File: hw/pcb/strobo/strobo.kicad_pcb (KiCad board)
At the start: 2 copper layers, 91 parts, among them J1 Conn_ARM_JTAG_SWD_10, SW1 SW_SPST, U1 ICM-20602, U2 STM32L051K8Ux, Y1 32kHz

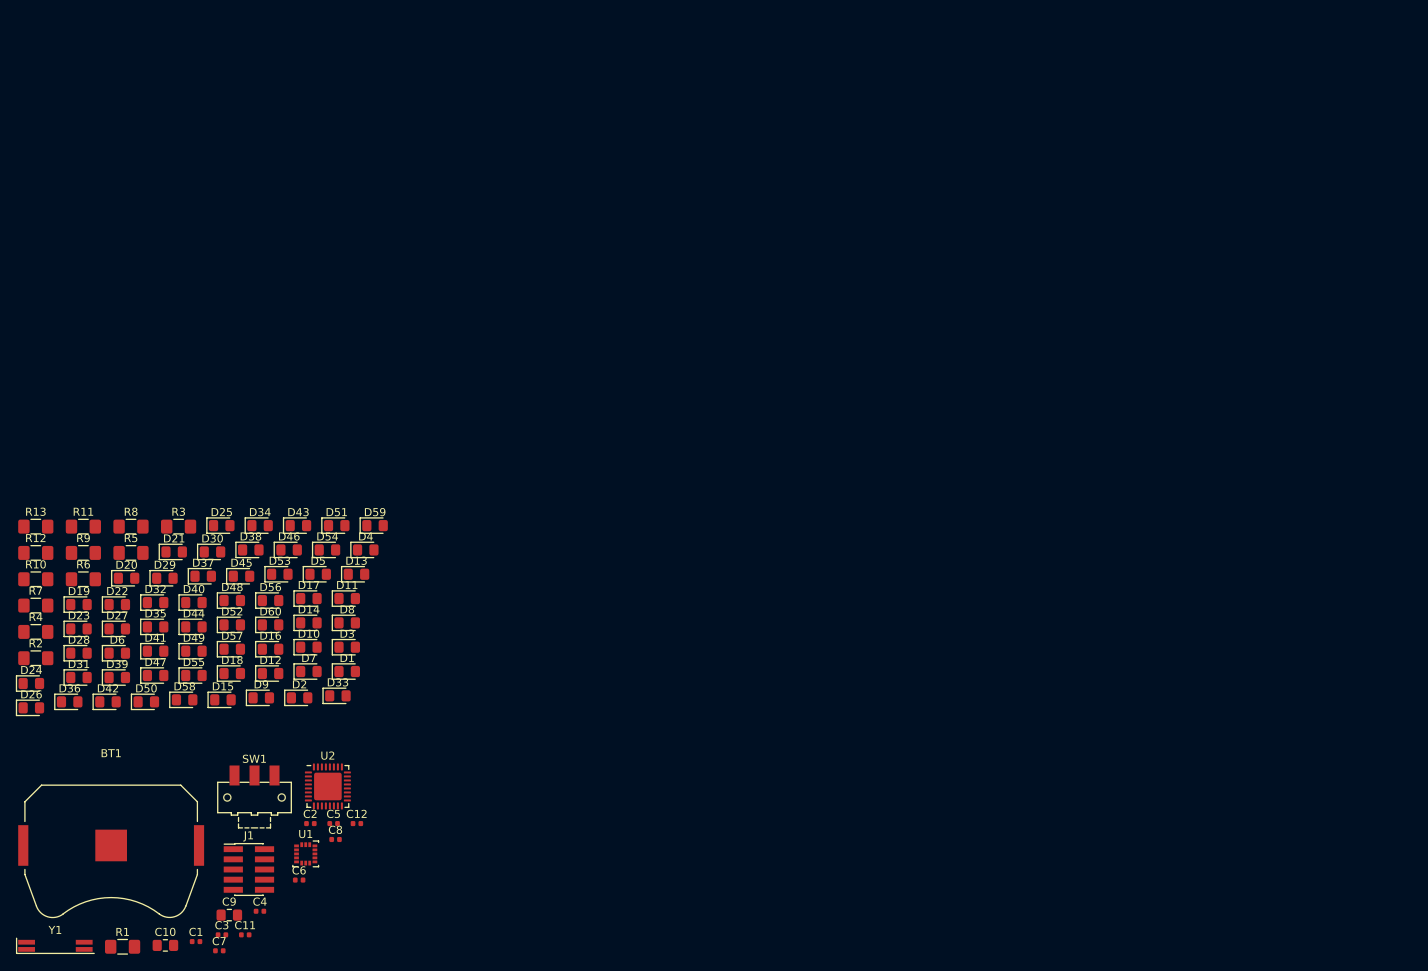
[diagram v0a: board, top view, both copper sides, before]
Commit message: initial led placement
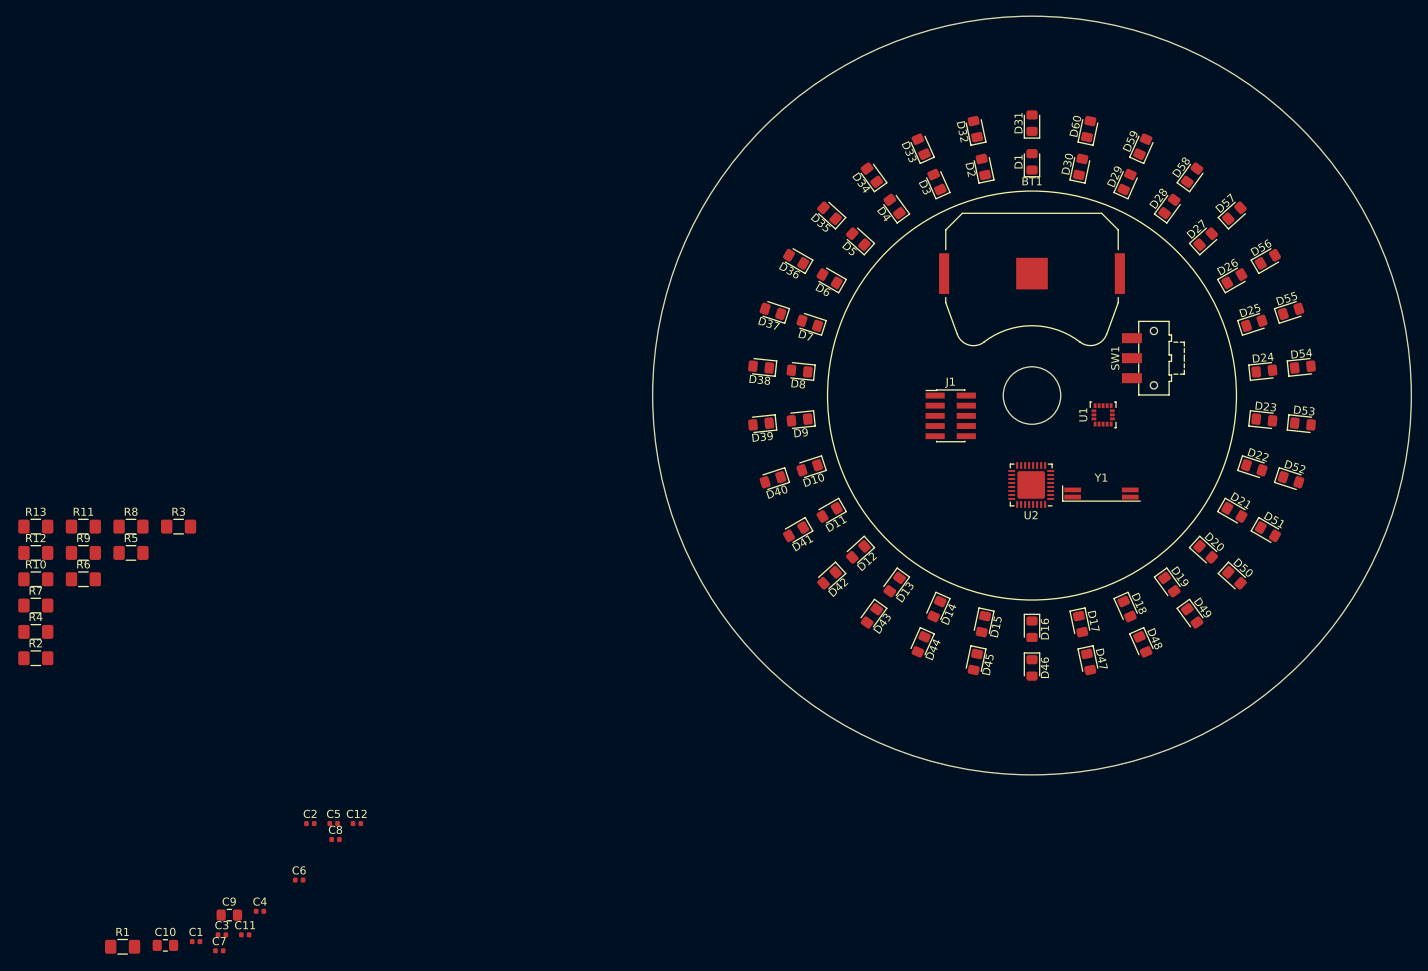
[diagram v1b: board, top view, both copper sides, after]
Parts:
- moved D26 159.7 mm to (226.0, 85.7), turned to 30 degrees
- moved D24 159.0 mm to (229.7, 97.3), turned to 6 degrees
- moved D23 150.5 mm to (229.7, 103.4), turned to 354 degrees
- moved D28 147.3 mm to (217.8, 76.7), turned to 54 degrees
- moved D27 144.5 mm to (222.4, 80.8), turned to 42 degrees
- moved D55 144.5 mm to (233.0, 89.8), turned to 18 degrees
- moved D22 143.1 mm to (228.4, 109.4), turned to 342 degrees
- moved Y1 142.5 mm to (209.3, 112.6)
- moved D58 142.0 mm to (220.7, 72.8), turned to 54 degrees
- moved D31 137.8 mm to (200.7, 66.3), turned to 90 degrees
- moved D50 136.9 mm to (226.0, 123.1), turned to 318 degrees
- moved D57 136.6 mm to (226.0, 77.5), turned to 42 degrees
- moved D19 136.3 mm to (217.8, 124.0), turned to 306 degrees
- moved BT1 135.5 mm to (200.7, 85.1)
- moved D20 134.9 mm to (222.4, 119.9), turned to 318 degrees
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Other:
- board outline added: 94.8 x 94.8 mm

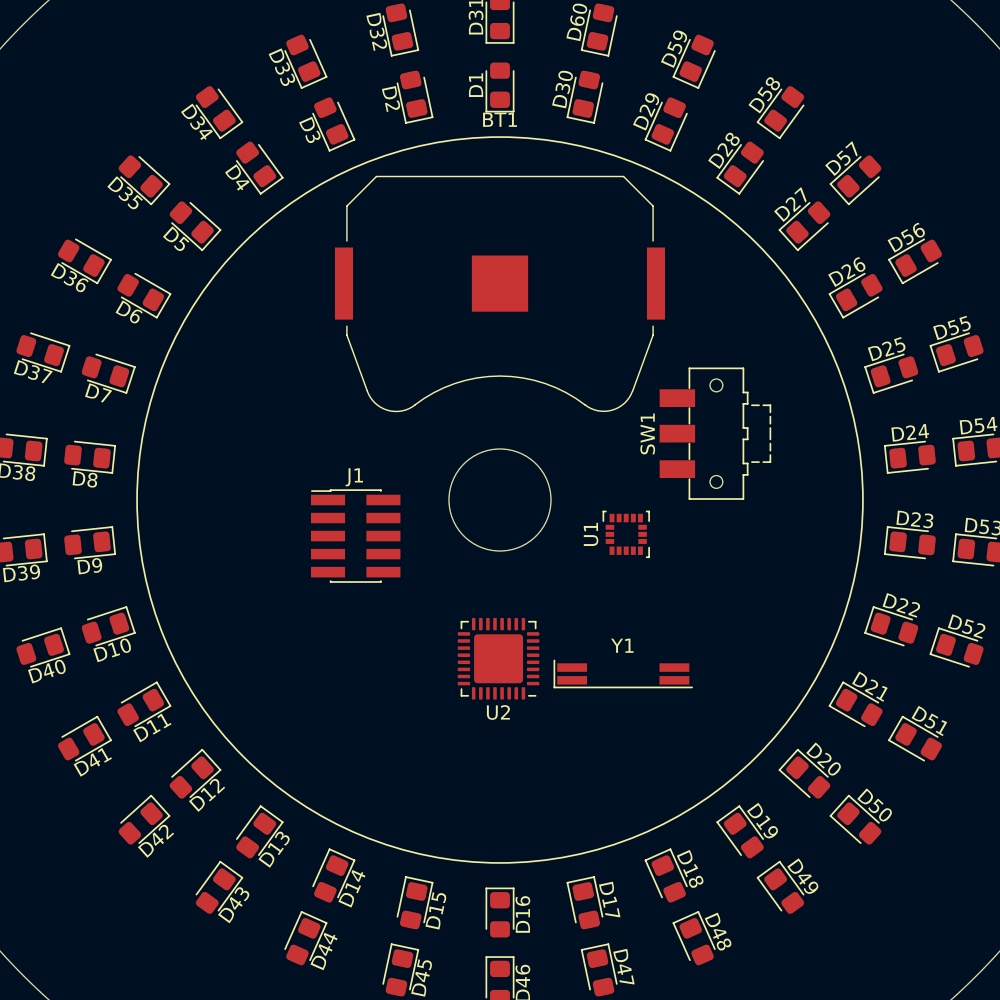
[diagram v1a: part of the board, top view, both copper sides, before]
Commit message: led tracks for inner ring
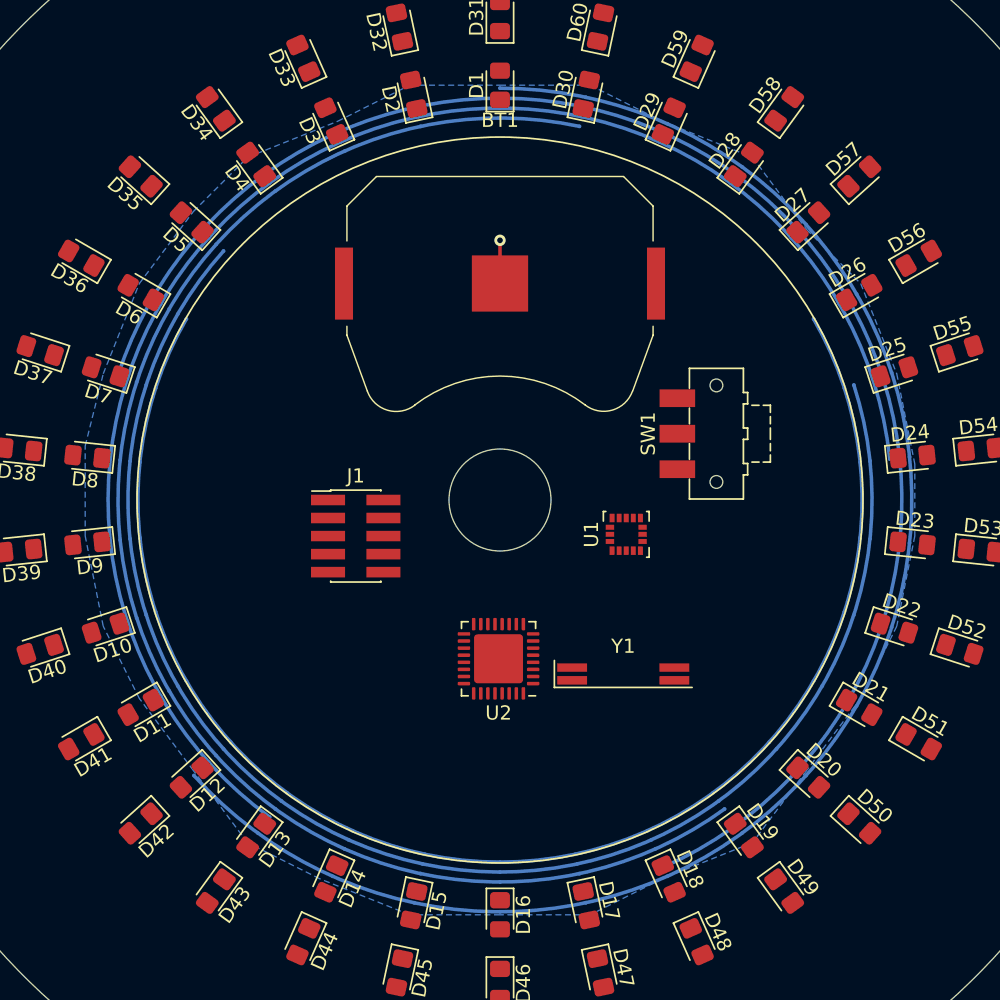
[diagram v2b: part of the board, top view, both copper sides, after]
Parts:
- added LED_Ring_Track: LED_Ring, strobo:LED_Ring, B.Cu at (200.7, 100.3)
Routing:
- net GND: track 0.00 -> 3.05 mm, vias 0 -> 1
- added copper zone on B.Cu, net GND
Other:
- net class Default: clearance 0.2 -> 0.1524
- rule trace_clearance: 0.2 -> 0.1524
- rule trace_min: 0.2 -> 0.1524
- rule via_min_drill: 0.3 -> 0.254
- rule via_min_size: 0.4 -> 0.508

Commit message: outer ring
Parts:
- turned LED_Ring_Track to 93 degrees
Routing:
- removed copper zone on B.Cu, net GND

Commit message: map ring tracks to schematic
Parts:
- removed LED_Ring_Track: LED_Ring, strobo:LED_Ring
- added U3: Ring_Tracks, strobo:LED_Ring, B.Cu at (200.7, 100.3)

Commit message: major routing
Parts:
- moved R13 146.5 mm to (219.7, 87.6), turned to 90 degrees
- moved R7 146.3 mm to (217.2, 87.6), turned to 90 degrees
- moved R12 143.7 mm to (219.7, 113.0), turned to 90 degrees
- moved R1 141.0 mm to (213.4, 106.7), turned to 180 degrees
- moved R6 135.5 mm to (217.2, 113.0), turned to 90 degrees
- moved R4 132.6 mm to (208.3, 119.4), turned to 180 degrees
- moved R10 132.2 mm to (208.3, 121.9), turned to 180 degrees
- moved C7 127.0 mm to (207.8, 104.1)
- moved C1 123.8 mm to (208.5, 116.6)
- moved C11 117.8 mm to (206.2, 112.3), turned to 180 degrees
- moved C10 117.7 mm to (194.1, 109.9)
- moved R2 117.2 mm to (184.2, 87.6), turned to 90 degrees
- moved C3 114.4 mm to (196.1, 106.7), turned to 180 degrees
- moved C6 113.2 mm to (207.8, 105.4), turned to 180 degrees
- moved C9 112.6 mm to (202.8, 118.6), turned to 90 degrees
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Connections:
- net /LED Matrix/LM_R_A renamed RA
- C6 pad 1: VDD -> Net-(C10-Pad2)
- C7 pad 2: VDD -> Net-(C10-Pad2)
- C8 pad 1: VDD -> Net-(C10-Pad2)
- D1 pad 1: /LED Matrix/LM_R_B -> RB
- D10 pad 1: /LED Matrix/LM_R_F -> RF
- D12 pad 1: /LED Matrix/LM_R_B -> RB
- D13 pad 1: /LED Matrix/LM_R_D -> RD
- D14 pad 1: /LED Matrix/LM_R_E -> RE
- D15 pad 1: /LED Matrix/LM_R_F -> RF
- D17 pad 1: /LED Matrix/LM_R_B -> RB
- D18 pad 1: /LED Matrix/LM_R_C -> RC
- D19 pad 1: /LED Matrix/LM_R_E -> RE
- D2 pad 1: /LED Matrix/LM_R_C -> RC
- D20 pad 1: /LED Matrix/LM_R_F -> RF
- D22 pad 1: /LED Matrix/LM_R_B -> RB
- D23 pad 1: /LED Matrix/LM_R_C -> RC
- D24 pad 1: /LED Matrix/LM_R_D -> RD
- D25 pad 1: /LED Matrix/LM_R_F -> RF
- D27 pad 1: /LED Matrix/LM_R_B -> RB
- D28 pad 1: /LED Matrix/LM_R_C -> RC
- D29 pad 1: /LED Matrix/LM_R_D -> RD
- D3 pad 1: /LED Matrix/LM_R_D -> RD
- D30 pad 1: /LED Matrix/LM_R_E -> RE
- D31 pad 1: /LED Matrix/LM_S_B -> SB
- D32 pad 1: /LED Matrix/LM_S_C -> SC
- D33 pad 1: /LED Matrix/LM_S_D -> SD
- D34 pad 1: /LED Matrix/LM_S_E -> SE
- D35 pad 1: /LED Matrix/LM_S_F -> SF
- D36 pad 1: /LED Matrix/LM_S_A -> SA
- D37 pad 1: /LED Matrix/LM_S_C -> SC
- D38 pad 1: /LED Matrix/LM_S_D -> SD
- D39 pad 1: /LED Matrix/LM_S_E -> SE
- D4 pad 1: /LED Matrix/LM_R_E -> RE
- D40 pad 1: /LED Matrix/LM_S_F -> SF
- D41 pad 1: /LED Matrix/LM_S_A -> SA
- D42 pad 1: /LED Matrix/LM_S_B -> SB
- D43 pad 1: /LED Matrix/LM_S_D -> SD
- D44 pad 1: /LED Matrix/LM_S_E -> SE
- D45 pad 1: /LED Matrix/LM_S_F -> SF
- D46 pad 1: /LED Matrix/LM_S_A -> SA
- D47 pad 1: /LED Matrix/LM_S_B -> SB
- D48 pad 1: /LED Matrix/LM_S_C -> SC
- D49 pad 1: /LED Matrix/LM_S_E -> SE
- D5 pad 1: /LED Matrix/LM_R_F -> RF
- D50 pad 1: /LED Matrix/LM_S_F -> SF
- D51 pad 1: /LED Matrix/LM_S_A -> SA
- D52 pad 1: /LED Matrix/LM_S_B -> SB
- D53 pad 1: /LED Matrix/LM_S_C -> SC
- D54 pad 1: /LED Matrix/LM_S_D -> SD
- D55 pad 1: /LED Matrix/LM_S_F -> SF
- D56 pad 1: /LED Matrix/LM_S_A -> SA
- D57 pad 1: /LED Matrix/LM_S_B -> SB
- D58 pad 1: /LED Matrix/LM_S_C -> SC
- D59 pad 1: /LED Matrix/LM_S_D -> SD
- D60 pad 1: /LED Matrix/LM_S_E -> SE
- D7 pad 1: /LED Matrix/LM_R_C -> RC
- D8 pad 1: /LED Matrix/LM_R_D -> RD
- D9 pad 1: /LED Matrix/LM_R_E -> RE
- R10 pad 1: /LED Matrix/LM_S_C -> SC
- R11 pad 1: /LED Matrix/LM_S_D -> SD
- R12 pad 1: /LED Matrix/LM_S_E -> SE
- R13 pad 1: /LED Matrix/LM_S_F -> SF
- R3 pad 1: /LED Matrix/LM_R_B -> RB
- R4 pad 1: /LED Matrix/LM_R_C -> RC
- R5 pad 1: /LED Matrix/LM_R_D -> RD
- R6 pad 1: /LED Matrix/LM_R_E -> RE
- R7 pad 1: /LED Matrix/LM_R_F -> RF
- R8 pad 1: /LED Matrix/LM_S_A -> SA
- R9 pad 1: /LED Matrix/LM_S_B -> SB
- U1 pad 1: VDD -> Net-(C10-Pad2)
- U1 pad 16: VDD -> Net-(C10-Pad2)
- U2 pad 19: /LED Matrix/LM_R_B -> SA
- U2 pad 20: /LED Matrix/LM_R_C -> RB
- U2 pad 21: /LED Matrix/LM_R_D -> SB
- U2 pad 22: /LED Matrix/LM_R_E -> RD
- U2 pad 25: /LED Matrix/LM_R_F -> SD
- U2 pad 26: /LED Matrix/LM_S_F -> RC
- U2 pad 27: /LED Matrix/LM_S_E -> SC
- U2 pad 28: /LED Matrix/LM_S_D -> RE
- U2 pad 29: /LED Matrix/LM_S_C -> Net-(U2-Pad29)
- U2 pad 30: /LED Matrix/LM_S_B -> Net-(U2-Pad30)
- U2 pad 32: /LED Matrix/LM_S_A -> Net-(U2-Pad32)
- U2 pad 6: Net-(U2-Pad6) -> SE
- U2 pad 7: Net-(U2-Pad7) -> RF
- U2 pad 8: Net-(U2-Pad8) -> SF
- U3 pad 10: /LED Matrix/LM_S_D -> SD
- U3 pad 11: /LED Matrix/LM_S_E -> SE
- U3 pad 12: /LED Matrix/LM_S_F -> SF
- U3 pad 13: /LED Matrix/LM_S_A -> SA
- U3 pad 2: /LED Matrix/LM_R_F -> RF
- U3 pad 3: /LED Matrix/LM_R_E -> RE
- U3 pad 4: /LED Matrix/LM_R_D -> RD
- U3 pad 5: /LED Matrix/LM_R_C -> RC
- U3 pad 6: /LED Matrix/LM_R_B -> RB
- U3 pad 8: /LED Matrix/LM_S_B -> SB
- U3 pad 9: /LED Matrix/LM_S_C -> SC
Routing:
- net SA: track 0.00 -> 64.9 mm, vias 0 -> 5
- net SF: track 0.00 -> 59.3 mm, vias 0 -> 6
- net Net-(C10-Pad2): track 0.00 -> 57.3 mm, vias 0 -> 8
- net SB: track 0.00 -> 56.4 mm, vias 0 -> 5
- net RA: track 0.00 -> 55.9 mm, vias 0 -> 5
- net RF: track 0.00 -> 48.1 mm, vias 0 -> 6
- net SC: track 0.00 -> 42.9 mm, vias 0 -> 7
- net VDD: track 0.00 -> 42.0 mm
- net SE: track 0.00 -> 39.9 mm, vias 0 -> 5
- net RB: track 0.00 -> 36.5 mm, vias 0 -> 5
- net RE: track 0.00 -> 34.8 mm, vias 0 -> 7
- net RC: track 0.00 -> 34.6 mm, vias 0 -> 7
- net SD: track 0.00 -> 33.4 mm, vias 0 -> 5
- net Net-(D41-Pad2): track 0.00 -> 32.4 mm, vias 0 -> 7
- net Net-(D46-Pad2): track 0.00 -> 27.4 mm, vias 0 -> 5
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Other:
- board size 94.8 x 94.8 mm -> 74 x 74 mm

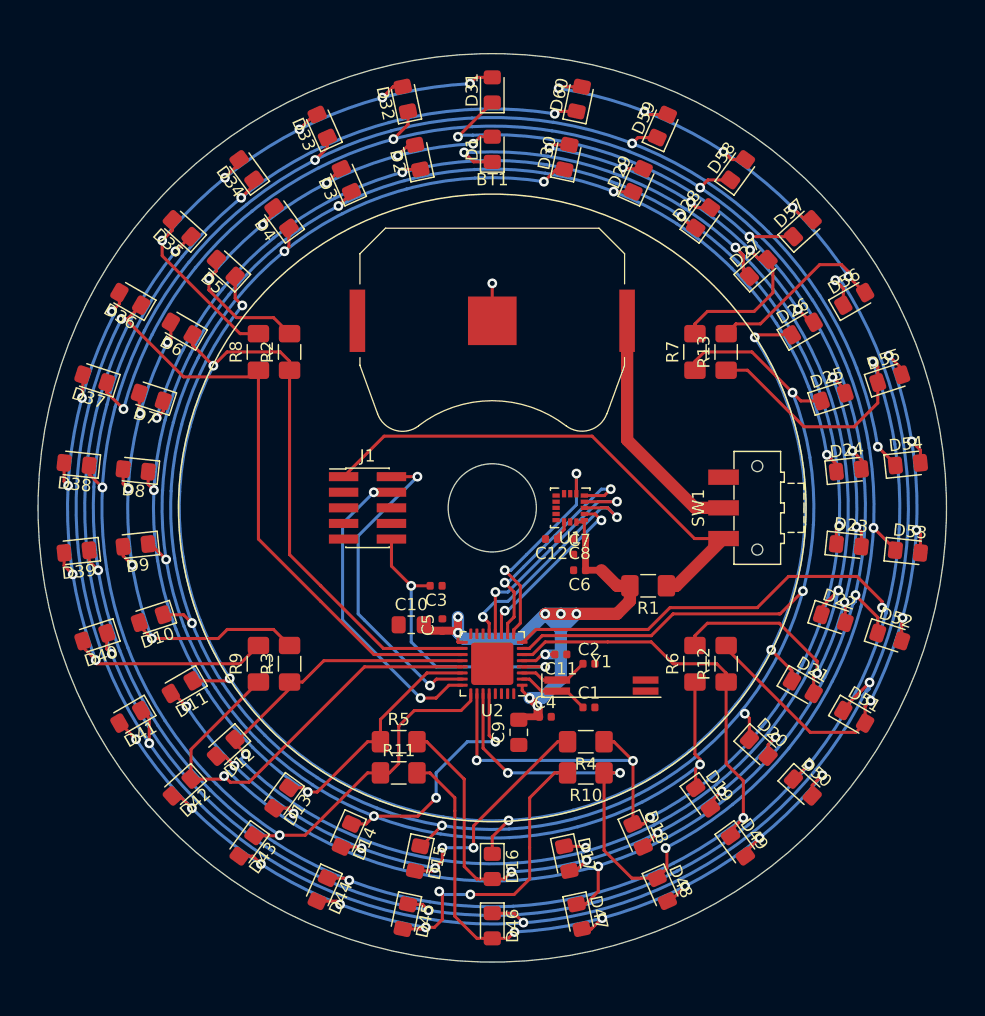
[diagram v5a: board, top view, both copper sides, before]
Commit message: move imu and pour gnd
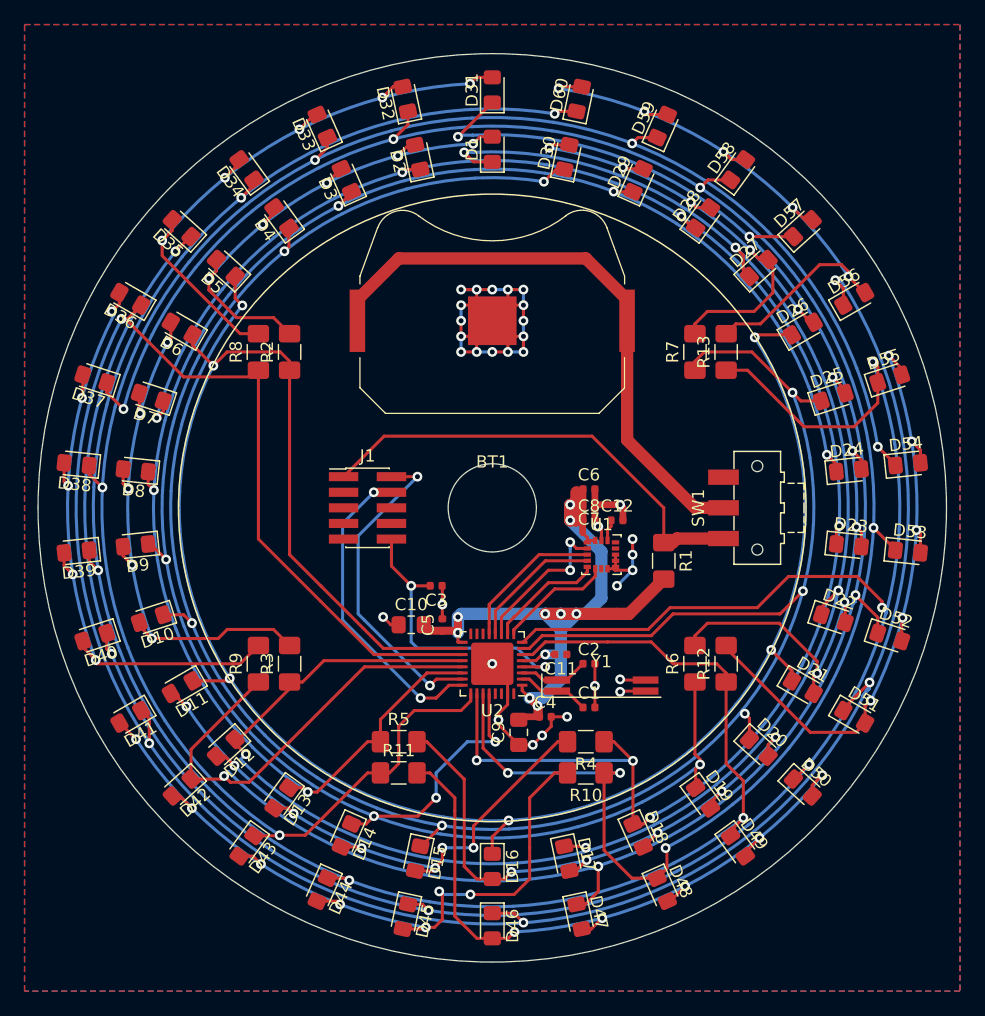
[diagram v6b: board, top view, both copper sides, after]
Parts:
- moved C6 6.65 mm to (208.5, 98.8), turned to 0 degrees
- moved C12 5.55 mm to (210.8, 101.3), turned to 0 degrees
- moved U1 4.58 mm to (209.6, 104.1), turned to 0 degrees
- moved C7 4.13 mm to (208.5, 100.1), turned to 180 degrees
- moved R1 2.40 mm to (214.6, 104.6), turned to 270 degrees
- moved C8 1.70 mm to (208.5, 101.3), turned to 0 degrees
- turned BT1 to 180 degrees
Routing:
- net GND: track 3.05 -> 90.4 mm, vias 1 -> 32
- net Net-(BT1-Pad1): track 19.9 -> 48.0 mm
- net Net-(C10-Pad2): track 57.3 -> 70.2 mm, vias 8 -> 10
- net ~CS: track 18.9 -> 9.48 mm, vias 2 -> 0
- net INT: track 18.2 -> 9.39 mm, vias 2 -> 0
- net MISO: track 19.0 -> 11.1 mm, vias 2 -> 0
- net MOSI: track 19.6 -> 12.1 mm, vias 2 -> 0
- net VDD: track 42.0 -> 37.7 mm
- net CLK: track 14.5 -> 12.4 mm
- added copper zone on B.Cu, net GND
- added copper zone on F.Cu, net GND
